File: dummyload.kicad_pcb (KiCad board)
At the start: 2 copper layers, 99.5 x 133 mm, 156 parts

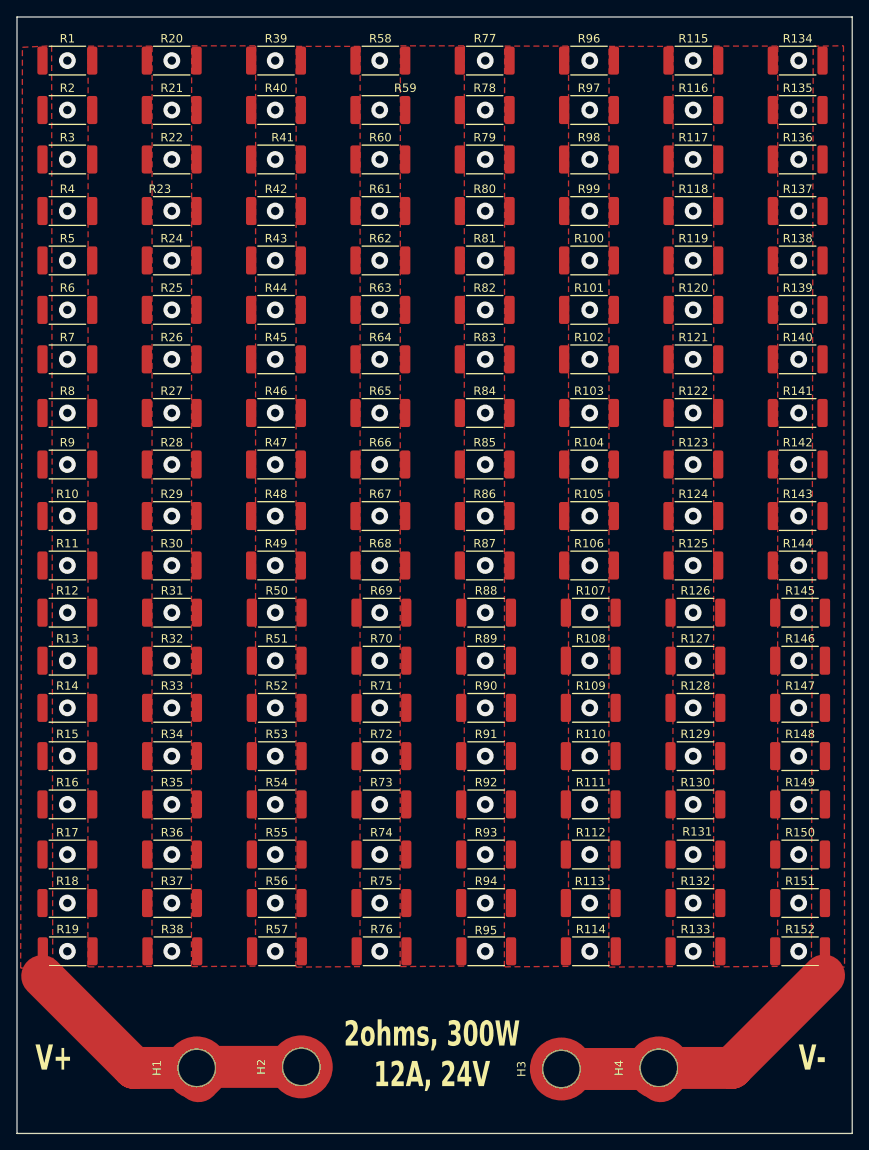
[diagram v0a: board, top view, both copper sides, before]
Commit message: made V+ and V- races thicker (8mm instead of 5).  This required movig the resistor banks slightly closer together.  Overall should reduce resistance of traces and zones without thermal impact
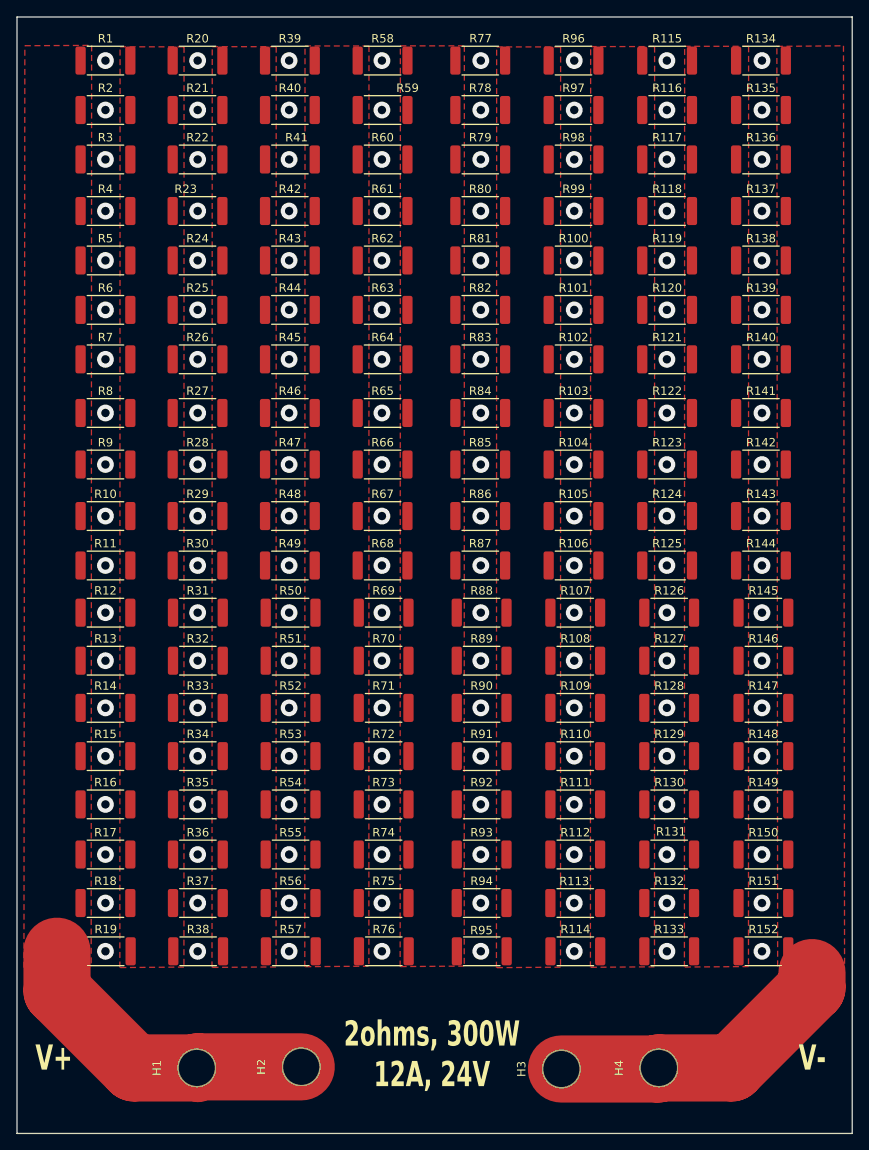
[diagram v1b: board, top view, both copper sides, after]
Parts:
- moved R1 4.54 mm to (52.0, 26.2)
- moved R10 4.54 mm to (52.0, 80.4)
- moved R11 4.54 mm to (52.0, 86.3)
- moved R12 4.54 mm to (52.0, 92.0)
- moved R13 4.54 mm to (52.0, 97.7)
- moved R14 4.54 mm to (52.0, 103.3)
- moved R15 4.54 mm to (52.0, 109.0)
- moved R16 4.54 mm to (52.0, 114.8)
- moved R17 4.54 mm to (52.0, 120.8)
- moved R18 4.54 mm to (52.0, 126.5)
- moved R19 4.54 mm to (52.1, 132.3)
- moved R2 4.54 mm to (52.0, 32.1)
- moved R3 4.54 mm to (52.0, 38.0)
- moved R4 4.54 mm to (52.0, 44.1)
- moved R5 4.54 mm to (52.0, 50.0)
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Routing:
- net /V+: track 35.6 -> 37.9 mm
